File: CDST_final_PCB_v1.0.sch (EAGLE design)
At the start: 39 parts, among them IC1 MIC_I2S_SPH0645, U1 AD8232ACPZ-R7

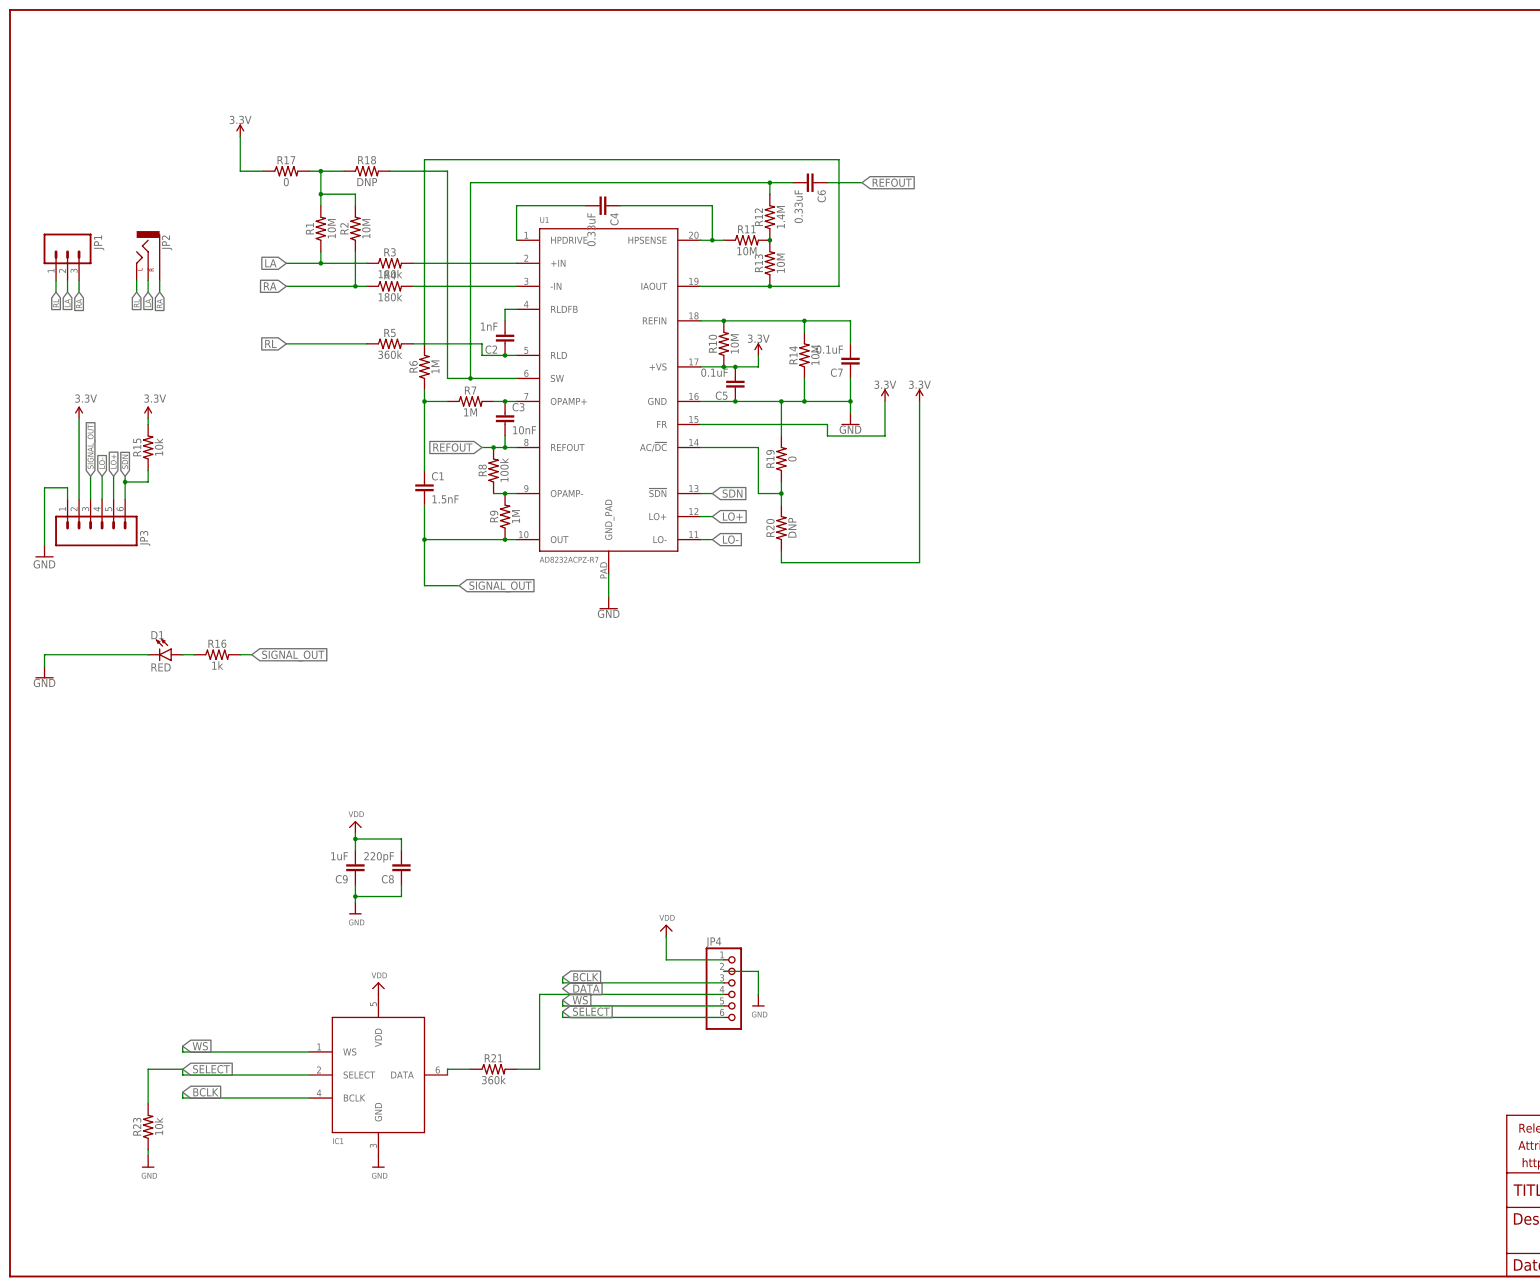
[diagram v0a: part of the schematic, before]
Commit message: added power electronics
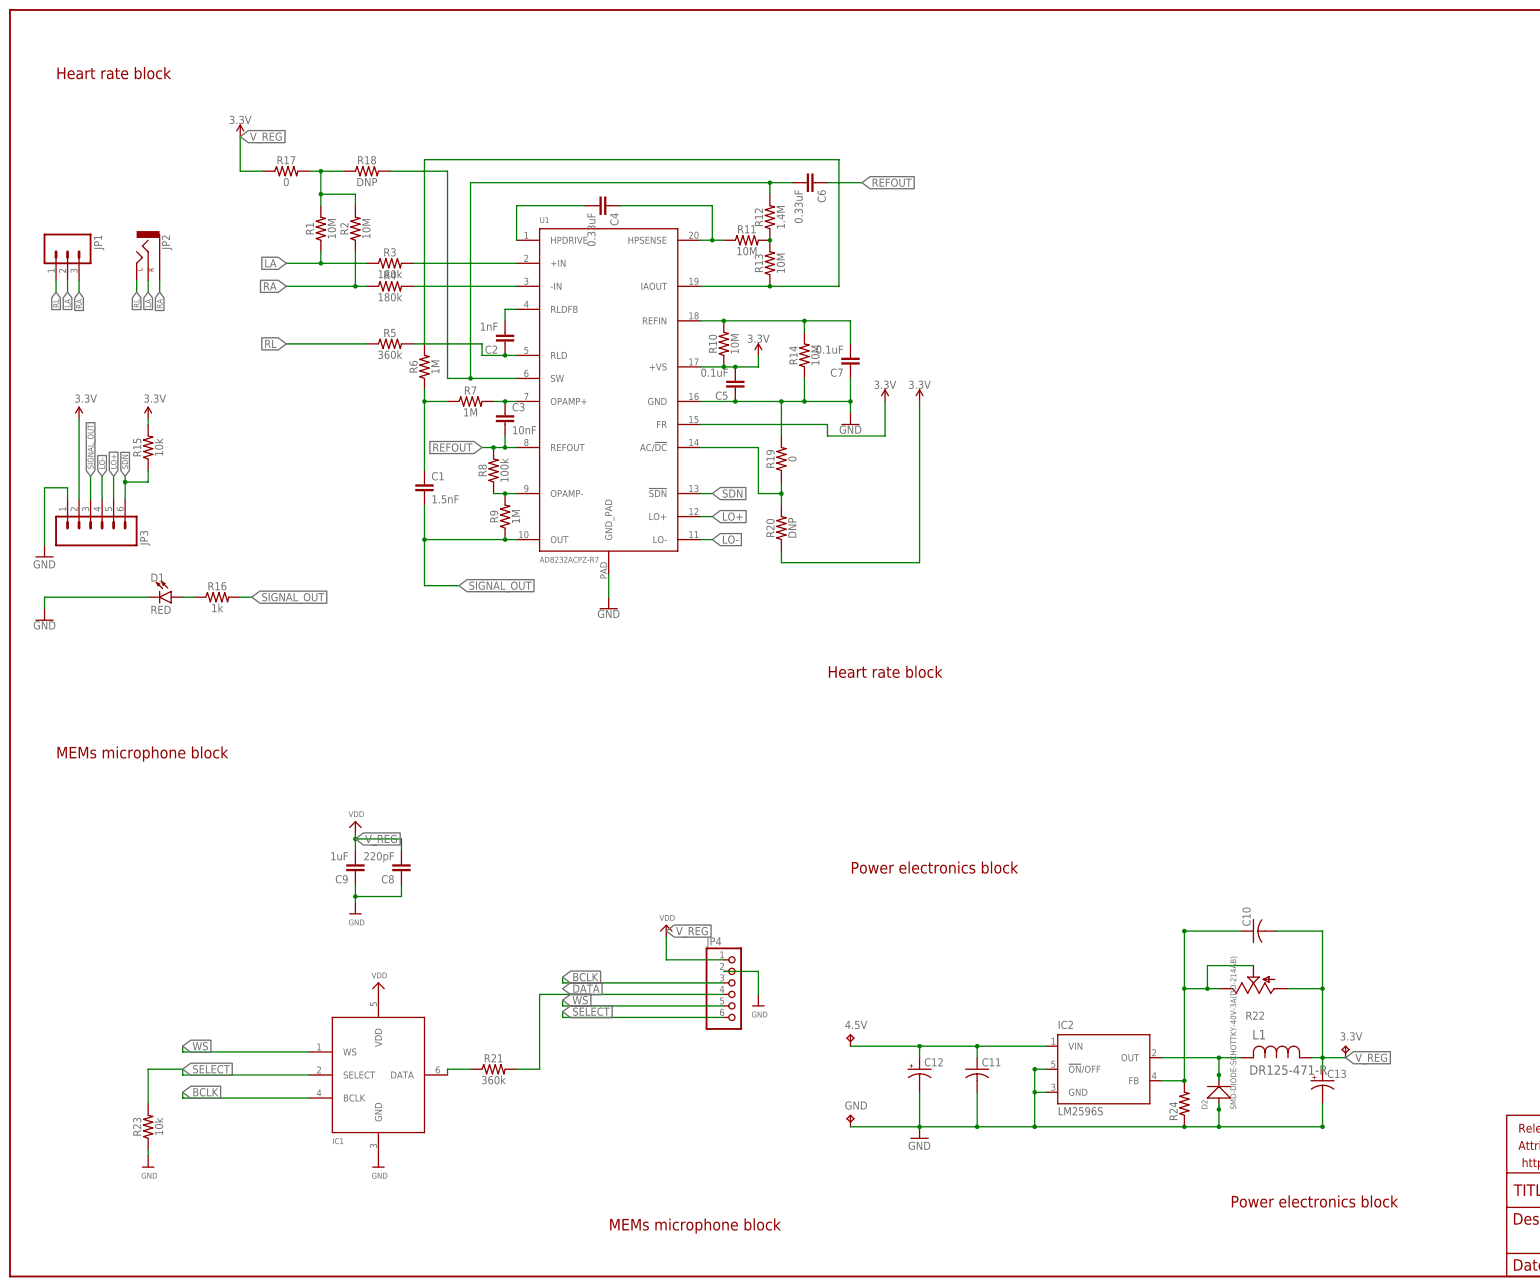
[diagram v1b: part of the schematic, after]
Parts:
- added 3.3V, 4.5V, GND: TPTP20SQ, testpad:TPTP20SQ
- added C10, C11: (no value), rcl:C-USC0402
- added C12, C13: (no value), rcl:CPOL-USSANYO_SMD_F8
- added D2: SMD-DIODE-SCHOTTKY-40V-3A(DO-214AB), SMD-DIODE-SCHOTTKY-40V-3A_DO-214AB_:SMD-DIODE-SCHOTTKY-40V-3A(DO-214AB)
- added IC2: LM2596S, national-semiconductor:LM2596S
- added L1: DR125-471-R, DR125-471-R:DR125-471-R
- added R22: (no value), pot:TRIM_US-RJ9W
- added R24: (no value), rcl:R-US_MELF0204W
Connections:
- new net N$12: C10.1, IC2.FB, R22.E, R22.S, R24.2
- new net N$21: D2.-, IC2.OUT, L1.2
- new net N$6: 4.5V.TP, C11.1, C12.+, IC2.VIN
- new net V_REG: 3.3V.TP, C10.2, C13.+, C8.2, C9.2, JP4.1, L1.1, R17.1, R22.A
- net GND: now also C11.2, C12.-, C13.-, D2.+, GND.TP, IC2.!ON!/OFF, IC2.GND, R24.1
- net VCC: no longer R17.1
- net VDD: no longer C8.2, C9.2, JP4.1
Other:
- note added: "Heart rate block"
- note added: "MEMs microphone block"
- note added: "Power electronics block"
- moved on the sheet: D1, R16

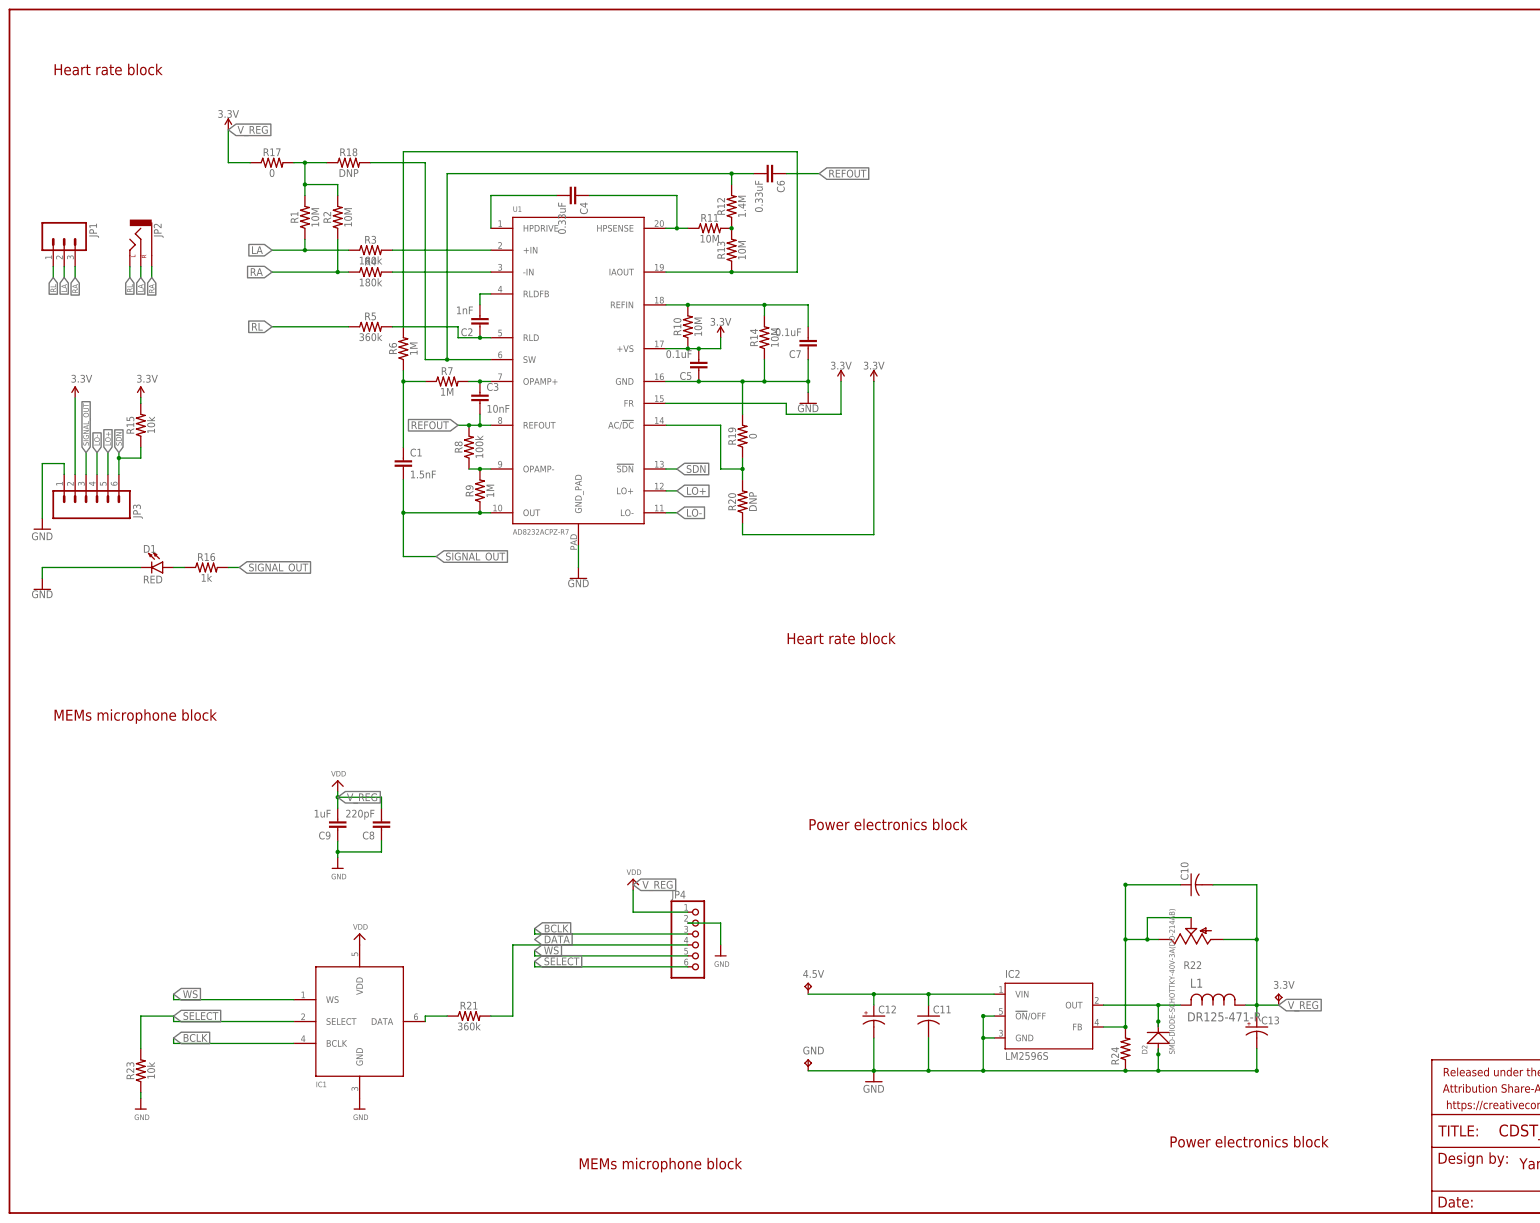
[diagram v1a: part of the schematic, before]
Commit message: fixed ERC errors
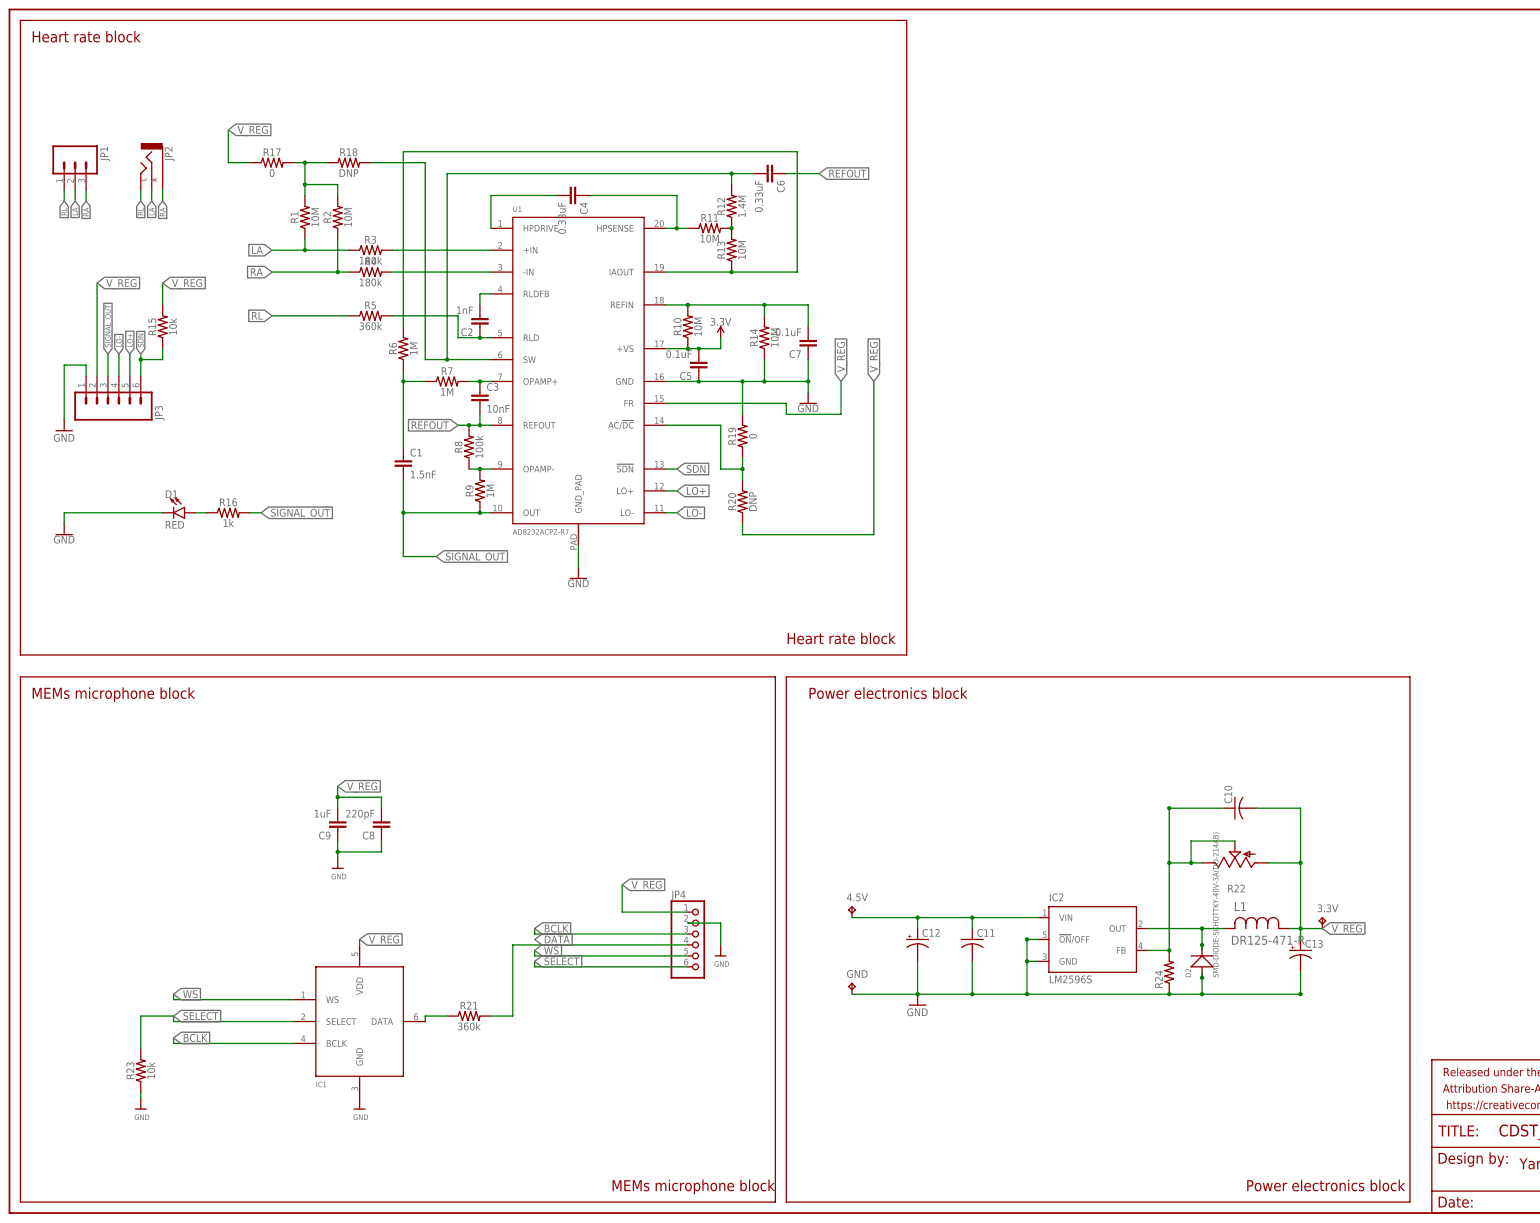
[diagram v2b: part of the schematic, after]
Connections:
- removed net 3.3V: JP3.2, R15.2
- removed net N$9: C3.2, R8.2, U1.REFOUT
- removed net VDD: IC1.VDD
- net REFOUT: now also C3.2, R8.2, U1.REFOUT
- net VCC: no longer R20.1, U1.FR
- net V_REG: now also IC1.VDD, JP3.2, R15.2, R20.1, U1.FR
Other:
- moved on the sheet: 3.3V, 4.5V, C10, C11, C12, C13, D1, D2, GND, IC2, JP1, JP2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
